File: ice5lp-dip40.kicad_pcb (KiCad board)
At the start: 2 copper layers, 17.8 x 50.8 mm, 6 parts, among them J1 Conn_02x04_Odd_Even, J2 Conn_01x20, J3 Conn_01x20, U1 AT25D011-SSHF, U2 MIC5355-S4YMME, U3 ICE5LP4K-SG48

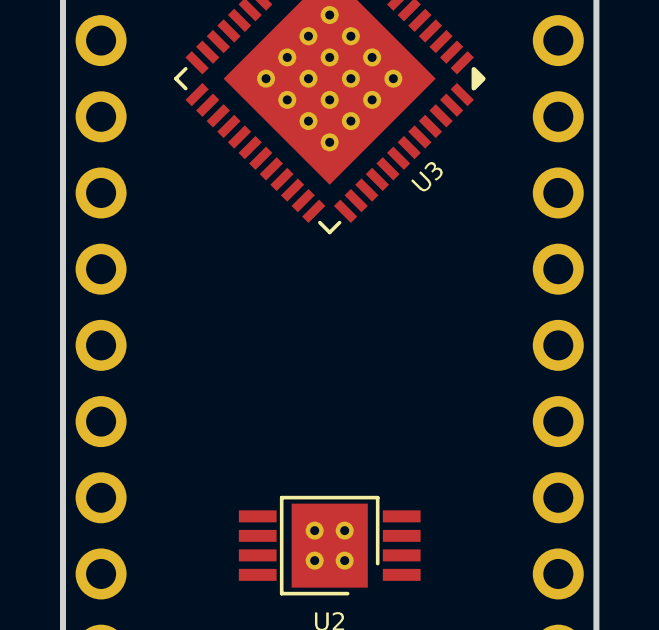
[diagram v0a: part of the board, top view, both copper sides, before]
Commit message: Add RGB LED and assign some FPGA IO to pin headers
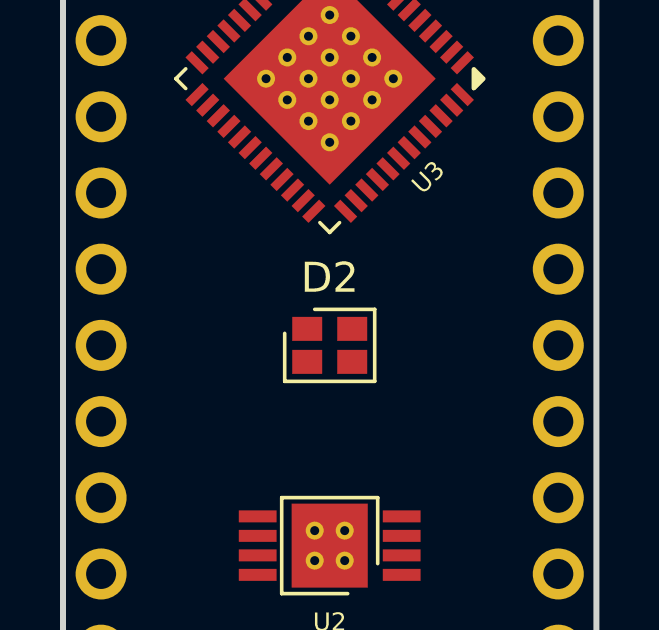
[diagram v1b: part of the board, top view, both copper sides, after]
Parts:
- added D2: CLMVC-FKC-CGJJM569aBB7a343, esynr3z_LED:LED_Cree-PLCC4_2x2mm_CW, F.Cu at (195.6, 91.4)
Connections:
- net Net-(J2-Pad10) renamed IOB_38B
- net Net-(J2-Pad11) renamed IOB_41A
- net Net-(J2-Pad12) renamed IOB_42B
- net Net-(J2-Pad13) renamed IOB_43A
- net Net-(J2-Pad14) renamed IOB_44B
- net Net-(J2-Pad15) renamed IOB_46B
- net Net-(J2-Pad16) renamed IOB_48B
- net Net-(J2-Pad17) renamed IOB_45A
- net Net-(J2-Pad18) renamed IOB_50B
- net Net-(J2-Pad7) renamed IOB_37A
- net Net-(J2-Pad8) renamed IOB_36B
- net Net-(J2-Pad9) renamed IOB_39A
- J2 pad 1: Net-(J2-Pad1) -> GND
- J2 pad 19: Net-(J2-Pad19) -> +5V
- J2 pad 2: Net-(J2-Pad2) -> IOB_24A
- J2 pad 20: Net-(J2-Pad20) -> GND
- J2 pad 3: Net-(J2-Pad3) -> IOB_31B
- J2 pad 4: Net-(J2-Pad4) -> IOB_29B
- J2 pad 5: Net-(J2-Pad5) -> IOB_25B
- J2 pad 6: Net-(J2-Pad6) -> IOB_23B
- J3 pad 1: Net-(J3-Pad1) -> GND
- J3 pad 19: Net-(J3-Pad19) -> +5V
- J3 pad 20: Net-(J3-Pad20) -> GND

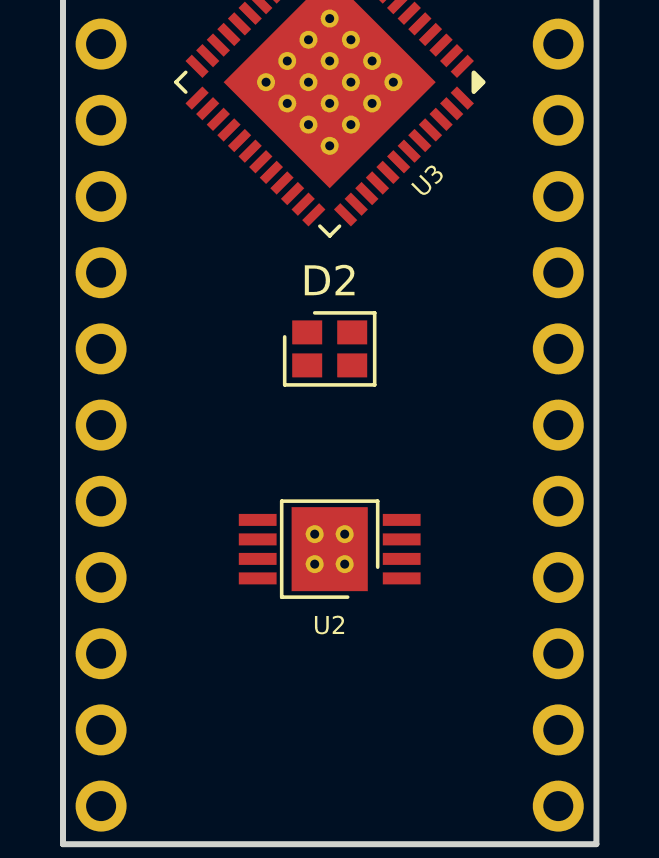
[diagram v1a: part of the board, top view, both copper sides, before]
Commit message: Add oscillator
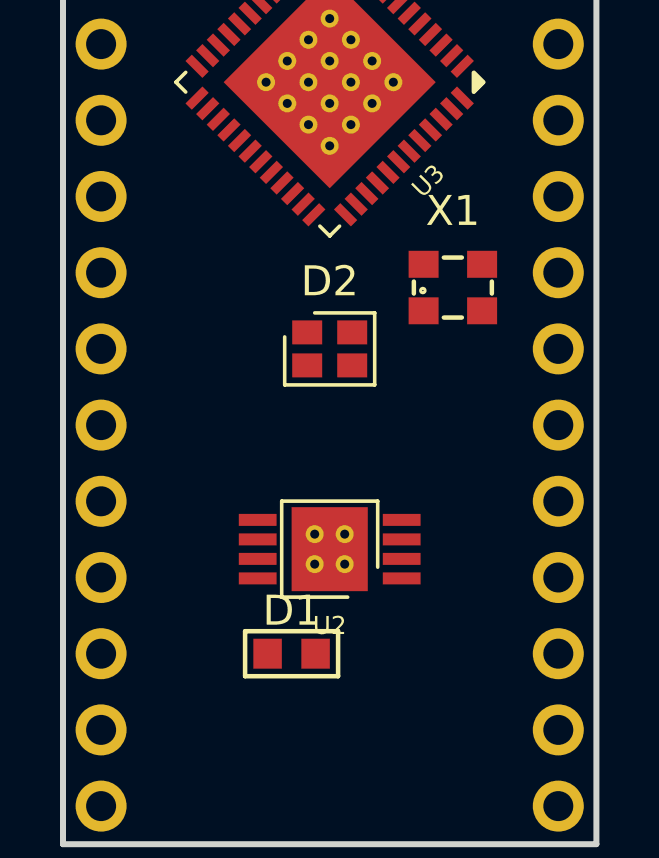
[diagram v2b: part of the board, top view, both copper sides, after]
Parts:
- added D1: CDBU0520, esynr3z_Diode:SOD-523F, F.Cu at (194.3, 101.6)
- added X1: ECS-2520MV-500-BN-TR, esynr3z_Oscillator:ECS-2520MV_4Pin_2.5x2.0mm, F.Cu at (199.7, 89.4)
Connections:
- J2 pad 10: IOB_38B -> IOT_38B
- J2 pad 11: IOB_41A -> IOT_41A
- J2 pad 13: IOB_43A -> IOT_43A
- J2 pad 14: IOB_44B -> IOT_44B
- J2 pad 15: IOB_46B -> IOT_46B
- J2 pad 16: IOB_48B -> IOT_48B
- J2 pad 17: IOB_45A -> IOT_45A
- J2 pad 18: IOB_50B -> IOT_50B
- J2 pad 5: IOB_25B -> Net-(J2-Pad5)
- J2 pad 7: IOB_37A -> IOT_37A
- J2 pad 8: IOB_36B -> IOT_36B
- J2 pad 9: IOB_39A -> IOT_39A
- U3 pad 20: IOB_25B -> ICE_CLK

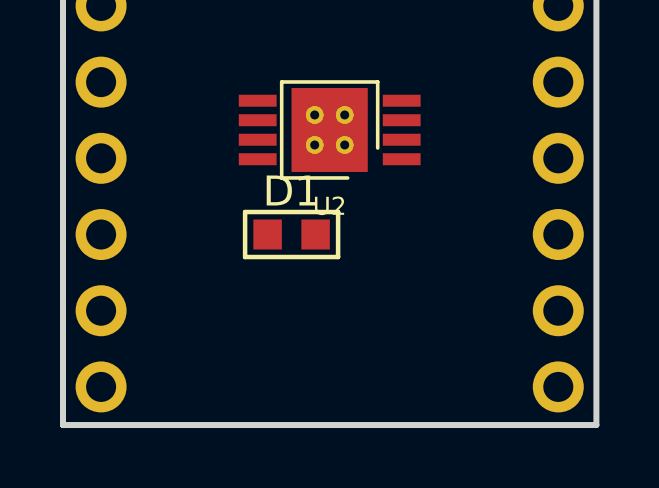
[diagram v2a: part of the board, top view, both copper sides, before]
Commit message: Add USB connector
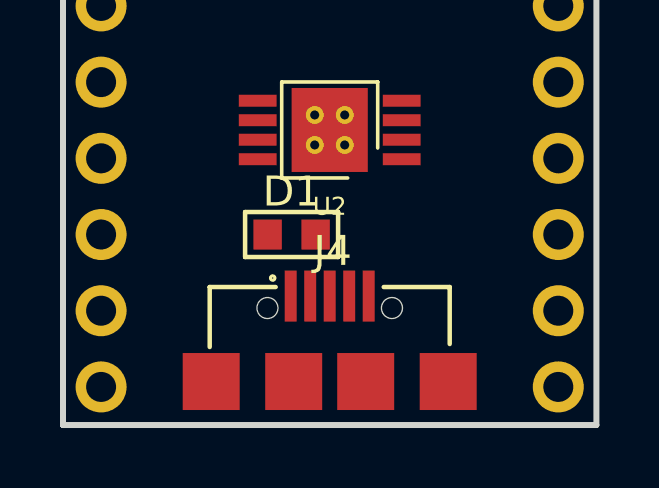
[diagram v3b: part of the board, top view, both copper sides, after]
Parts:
- added J4: USB_B_Micro, esynr3z_ConnectorUSB:USB_Micro-B_Wurth_629105136821, F.Cu at (195.6, 108.0)
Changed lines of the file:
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@@
     (tracks 0)
     (zones 0)
-    (modules 9)
-    (nets 74)
+    (modules 10)
+    (nets 77)
   )
   (page A4)
@@
     (31 B.Cu signal)
     (36 B.SilkS user hide)
-    (37 F.SilkS user hide)
+    (37 F.SilkS user)
     (38 B.Mask user)
     (39 F.Mask user)
@@
   (net 72 "Net-(D1-Pad1)")
   (net 73 ICE_CLK)
+  (net 74 "Net-(J4-Pad2)")
+  (net 75 "Net-(J4-Pad3)")
+  (net 76 "Net-(J4-Pad4)")
   (net_class Default "This is the default net class."
     (clearance 0.2)
@@
     (add_net "Net-(J3-Pad8)")
     (add_net "Net-(J3-Pad9)")
+    (add_net "Net-(J4-Pad2)")
+    (add_net "Net-(J4-Pad3)")
+    (add_net "Net-(J4-Pad4)")
     (add_net "Net-(R2-Pad2)")
     (add_net "Net-(R4-Pad2)")
@@
       (at (xyz 0 0 0))
       (scale (xyz 1 1 1))
+      (rotate (xyz 0 0 0))
+    )
+  )
+  (module esynr3z_ConnectorUSB:USB_Micro-B_Wurth_629105136821 (layer F.Cu)
+    (at 195.58 107.95)
+    (descr "USB Micro-B receptacle")
+    (tags "usb micro receptacle")
+    (attr smd)
+    (fp_text reference J4 (at 0.1 -5.8) (layer F.SilkS)
+      (effects (font (size 1 1) (thickness 0.15)))
+    )
+    (fp_text value USB_B_Micro (at 0 5.6) (layer F.Fab)
+      (effects (font (size 1 1) (thickness 0.15)))
+    )
+    (fp_line (start -4 -4.6) (end -4 1.3) (layer F.Fab) (width 0.15))
+    (fp_line (start -4 -0.65) (end -3.7 -0.65) (layer F.Fab) (width 0.15))
+    (fp_line (start -4 1.3) (end 4 1.3) (layer F.Fab) (width 0.15))
+    (fp_line (start 3.7 -0.65) (end 4 -0.65) (layer F.Fab) (width 0.15))
+    (fp_line (start 4 1.3) (end 4 -4.6) (layer F.Fab) (width 0.15))
+    (fp_line (start 4 -4.6) (end -4 -4.6) (layer F.Fab) (width 0.15))
+    (fp_line (start -2.7 0) (end 2.7 0) (layer F.Fab) (width 0.15))
+    (fp_line (start -1.075 -4.825) (end -1.3 -4.65) (layer F.Fab) (width 0.15))
+    (fp_line (start -1.3 -4.65) (end -1.525 -4.825) (layer F.Fab) (width 0.15))
+    (fp_line (start -1.525 -4.825) (end -1.525 -5.05) (layer F.Fab) (width 0.15))
+    (fp_line (start -1.525 -5.05) (end -1.075 -5.05) (layer F.Fab) (width 0.15))
+    (fp_line (start -1.075 -5.05) (end -1.075 -4.825) (layer F.Fab) (width 0.15))
+    (fp_line (start -4 -4.6) (end -4 -2.6) (layer F.SilkS) (width 0.15))
+    (fp_line (start 4 -2.7) (end 4 -4.6) (layer F.SilkS) (width 0.15))
+    (fp_line (start -1.8 -4.6) (end -4 -4.6) (layer F.SilkS) (width 0.15))
+    (fp_line (start 1.8 -4.6) (end 4 -4.6) (layer F.SilkS) (width 0.15))
+    (fp_line (start -5 -5.1) (end -5 1.4) (layer F.CrtYd) (width 0.05))
+    (fp_line (start -5 1.4) (end 5 1.4) (layer F.CrtYd) (width 0.05))
+    (fp_line (start 5 1.4) (end 5 -5.1) (layer F.CrtYd) (width 0.05))
+    (fp_line (start 5 -5.1) (end -5 -5.1) (layer F.CrtYd) (width 0.05))
+    (fp_text user %R (at 0 -2.75) (layer F.Fab)
+      (effects (font (size 1 1) (thickness 0.15)))
+    )
+    (fp_text user "PCB Edge" (at 0 -0.05) (layer Dwgs.User)
+      (effects (font (size 0.5 0.5) (thickness 0.08)))
+    )
+    (fp_circle (center -1.9 -4.9) (end -1.85 -4.9) (layer F.SilkS) (width 0.15))
+    (pad 1 smd rect (at -1.3 -4.3) (size 0.4 1.7) (layers F.Cu F.Paste F.Mask)
+      (net 32 +5V))
+    (pad 2 smd rect (at -0.65 -4.3) (size 0.4 1.7) (layers F.Cu F.Paste F.Mask)
+      (net 74 "Net-(J4-Pad2)"))
+    (pad 3 smd rect (at 0 -4.3) (size 0.4 1.7) (layers F.Cu F.Paste F.Mask)
+      (net 75 "Net-(J4-Pad3)"))
+    (pad 4 smd rect (at 0.65 -4.3) (size 0.4 1.7) (layers F.Cu F.Paste F.Mask)
+      (net 76 "Net-(J4-Pad4)"))
+    (pad 5 smd rect (at 1.3 -4.3) (size 0.4 1.7) (layers F.Cu F.Paste F.Mask)
+      (net 2 GND))
+    (pad "" np_thru_hole oval (at -2.075 -3.9) (size 0.7 0.7) (drill 0.7) (layers *.Cu *.Mask))
+    (pad "" np_thru_hole oval (at 2.075 -3.9) (size 0.7 0.7) (drill 0.7) (layers *.Cu *.Mask))
+    (pad 6 smd rect (at 1.2 -1.45) (size 1.9 1.9) (layers F.Cu F.Paste F.Mask)
+      (net 2 GND))
+    (pad 6 smd rect (at 3.95 -1.45) (size 1.9 1.9) (layers F.Cu F.Paste F.Mask)
+      (net 2 GND))
+    (pad 6 smd rect (at -1.2 -1.45) (size 1.9 1.9) (layers F.Cu F.Paste F.Mask)
+      (net 2 GND))
+    (pad 6 smd rect (at -3.95 -1.45) (size 1.9 1.9) (layers F.Cu F.Paste F.Mask)
+      (net 2 GND))
+    (model ${KISYS3DMOD}/Connector_USB.3dshapes/USB_Micro-B_Wuerth_629105150521.wrl
+      (at (xyz 0 0 0))
+      (scale (xyz 1 1 1))

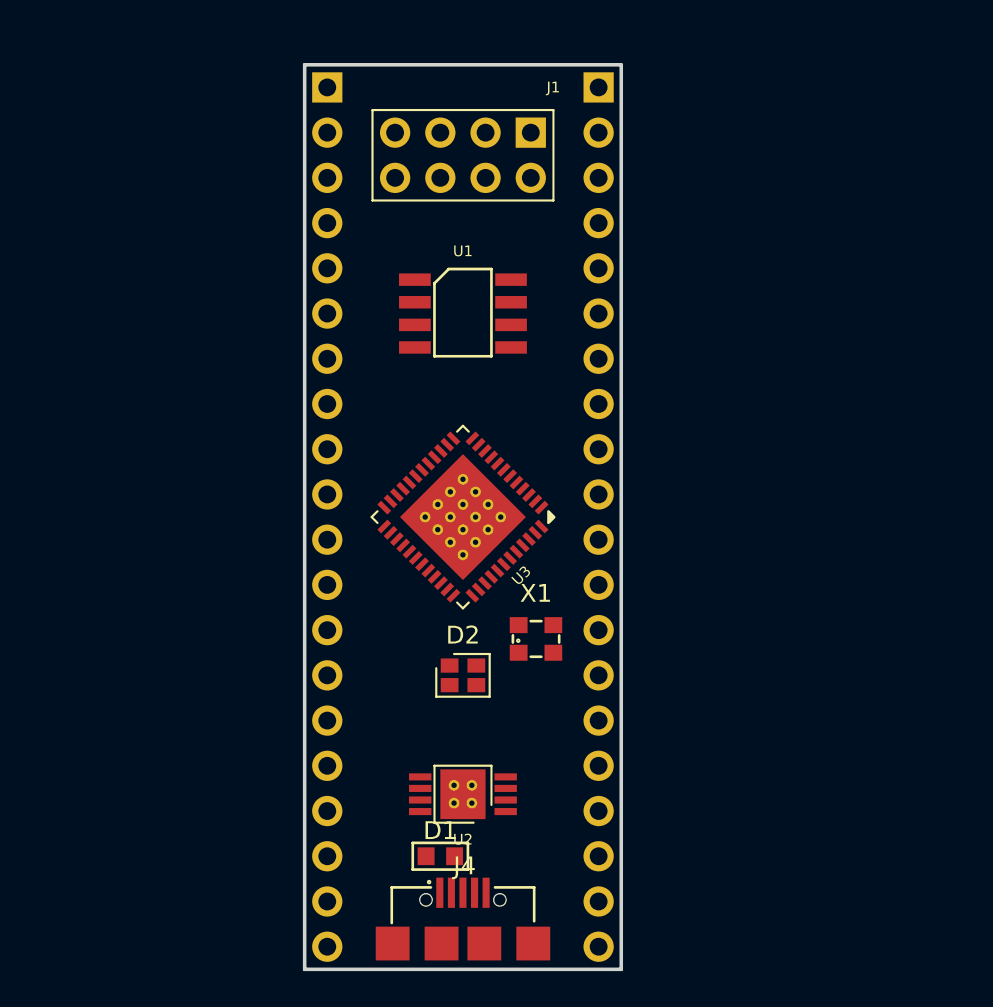
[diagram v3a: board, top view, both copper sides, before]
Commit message: Add footprints to some symbols and trace pin headers and buttons
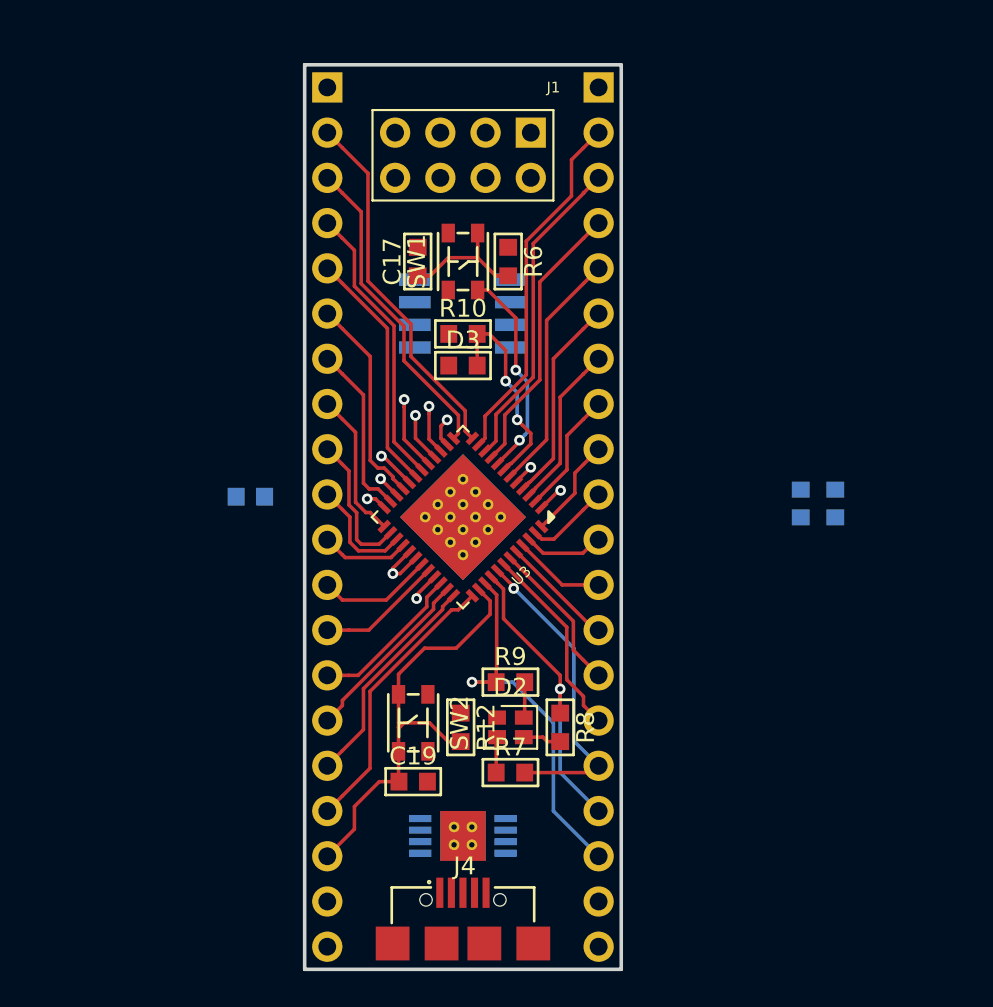
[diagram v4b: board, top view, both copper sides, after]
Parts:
- added C17: 100n, esynr3z_Passive:0603, F.Cu at (193.0, 68.2)
- added C19: 100n, esynr3z_Passive:0603, F.Cu at (192.8, 97.4)
- added D3: LED_GREEN, esynr3z_Passive:0603, F.Cu at (195.6, 74.0)
- added R10: 1k, esynr3z_Passive:0603, F.Cu at (195.6, 72.3)
- added R12: 10k, esynr3z_Passive:0603, F.Cu at (195.5, 94.4)
- added R6: 10k, esynr3z_Passive:0603, F.Cu at (198.1, 68.2)
- added R7: 82, esynr3z_Passive:0603, F.Cu at (198.2, 96.9)
- added R8: 22, esynr3z_Passive:0603, F.Cu at (201.0, 94.4)
- added R9: 22, esynr3z_Passive:0603, F.Cu at (198.2, 91.8)
- added SW1: SW_Push, esynr3z_Switch:PTS830, F.Cu at (195.6, 68.2)
- added SW2: SW_Push, esynr3z_Switch:PTS830, F.Cu at (192.8, 94.1)
- D1, U1, U2, X1: moved to B.Cu
- moved D1 22.8 mm to (183.6, 81.4)
- moved X1 17.6 mm to (215.5, 81.8)
- moved D2 3.96 mm to (198.2, 94.4)
- moved U2 2.34 mm to (195.6, 100.5), turned to 0 degrees
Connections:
- net IOT_50B renamed ICE_BTN
- J2 pad 12: IOB_42B -> IOT_42B
- J2 pad 2: IOB_24A -> IOB_22A
- J2 pad 3: IOB_31B -> IOB_24A
- J2 pad 4: IOB_29B -> IOB_31B
- J2 pad 5: Net-(J2-Pad5) -> IOB_29B
- J3 pad 10: Net-(J3-Pad10) -> IOB_2A
- J3 pad 11: Net-(J3-Pad11) -> IOB_0A
- J3 pad 12: Net-(J3-Pad12) -> IOB_5B
- J3 pad 13: Net-(J3-Pad13) -> IOB_3B
- J3 pad 14: Net-(J3-Pad14) -> IOT_49A
- J3 pad 15: Net-(J3-Pad15) -> IOT_51A
- J3 pad 16: Net-(J3-Pad16) -> RGB_R
- J3 pad 17: Net-(J3-Pad17) -> RGB_G
- J3 pad 18: Net-(J3-Pad18) -> RGB_B
- J3 pad 2: Net-(J3-Pad2) -> IOB_20A
- J3 pad 3: Net-(J3-Pad3) -> IOB_18A
- J3 pad 4: Net-(J3-Pad4) -> IOB_16A
- J3 pad 5: Net-(J3-Pad5) -> IOB_13B
- J3 pad 6: Net-(J3-Pad6) -> IOB_8A
- J3 pad 7: Net-(J3-Pad7) -> IOB_9B
- J3 pad 8: Net-(J3-Pad8) -> IOB_6A
- J3 pad 9: Net-(J3-Pad9) -> IOB_4A
- U3 pad 29: VCC_PLL -> VCC_CORE
- U3 pad 39: RGB2 -> RGB_B
- U3 pad 40: RGB1 -> RGB_G
- U3 pad 41: RGB0 -> RGB_R
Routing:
- net ICE_BTN: track 0.00 -> 24.8 mm
- net RGB_B: track 0.00 -> 21.3 mm, vias 0 -> 1
- net IOB_22A: track 0.00 -> 20.5 mm
- net IOB_20A: track 0.00 -> 20.3 mm
- net CRESET: track 0.00 -> 19.2 mm, vias 0 -> 2
- net IOB_18A: track 0.00 -> 18.2 mm
- net IOB_24A: track 0.00 -> 17.8 mm
- net RGB_R: track 0.00 -> 17.6 mm, vias 0 -> 1
- net RGB_G: track 0.00 -> 17.0 mm, vias 0 -> 1
- net IOB_31B: track 0.00 -> 16.1 mm
- net IOT_45A: track 0.00 -> 15.7 mm
- net IOB_16A: track 0.00 -> 15.6 mm
- net IOB_13B: track 0.00 -> 13.7 mm
- net IOB_29B: track 0.00 -> 13.7 mm
- net IOT_48B: track 0.00 -> 12.5 mm
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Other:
- net class Default: clearance 0.2 -> 0.17; via_dia 0.8 -> 0.6; via_drill 0.4 -> 0.3
- rule trace_clearance: 0.2 -> 0.17

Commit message: Update footprints
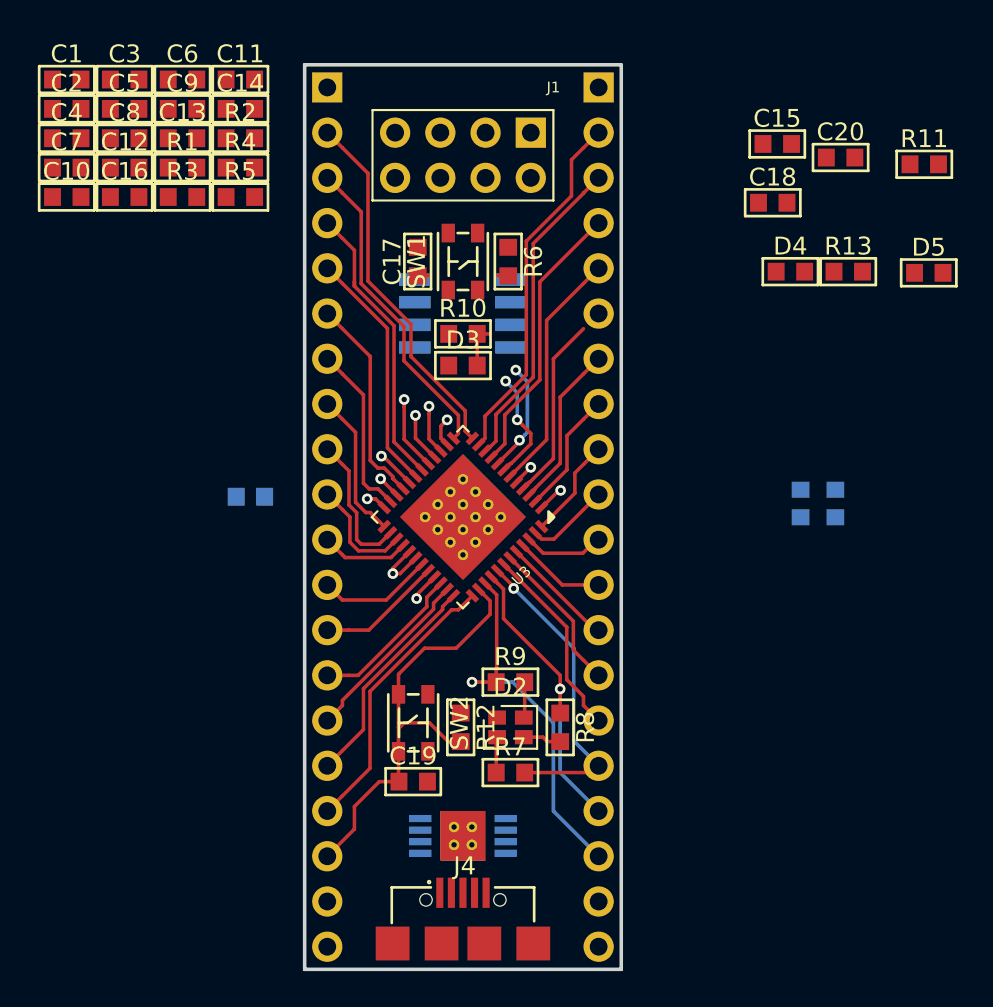
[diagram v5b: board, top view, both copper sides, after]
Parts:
- added C1: 1u, esynr3z_Capacitor:C_0603, F.Cu at (173.3, 58.0)
- added C10: 100n, esynr3z_Capacitor:C_0603, F.Cu at (173.3, 64.6)
- added C11: 100n, esynr3z_Capacitor:C_0603, F.Cu at (183.1, 58.0)
- added C12: 1u, esynr3z_Capacitor:C_0603, F.Cu at (176.6, 62.9)
- added C13: 100n, esynr3z_Capacitor:C_0603, F.Cu at (179.8, 61.3)
- added C14: 1u, esynr3z_Capacitor:C_0603, F.Cu at (183.1, 59.6)
- added C15: 100n, esynr3z_Capacitor:C_0603, F.Cu at (213.2, 61.6)
- added C16: 100n, esynr3z_Capacitor:C_0603, F.Cu at (176.6, 64.6)
- added C18: 100n, esynr3z_Capacitor:C_0603, F.Cu at (213.0, 64.9)
- added C2: 100n, esynr3z_Capacitor:C_0603, F.Cu at (173.3, 59.6)
- added C20: 10u, esynr3z_Capacitor:C_0603, F.Cu at (216.8, 62.4)
- added C3: 2.2u, esynr3z_Capacitor:C_0603, F.Cu at (176.6, 58.0)
- added C4: 100n, esynr3z_Capacitor:C_0603, F.Cu at (173.3, 61.3)
- added C5: 1u, esynr3z_Capacitor:C_0603, F.Cu at (176.6, 59.6)
- added C6: 100n, esynr3z_Capacitor:C_0603, F.Cu at (179.8, 58.0)
- added C7: 2.2u, esynr3z_Capacitor:C_0603, F.Cu at (173.3, 62.9)
- added C8: 2.2u, esynr3z_Capacitor:C_0603, F.Cu at (176.6, 61.3)
- added C9: 1u, esynr3z_Capacitor:C_0603, F.Cu at (179.8, 59.6)
- added D4: LED_RED, esynr3z_LED:LED_0603, F.Cu at (214.0, 68.8)
- added D5: LED_ORANGE, esynr3z_LED:LED_0603, F.Cu at (221.7, 68.8)
- added R1: 10k, esynr3z_Resistor:R_0603, F.Cu at (179.8, 62.9)
- added R11: 2.2k, esynr3z_Resistor:R_0603, F.Cu at (221.5, 62.7)
- added R13: 1k, esynr3z_Resistor:R_0603, F.Cu at (217.2, 68.8)
- added R2: 10k, esynr3z_Resistor:R_0603, F.Cu at (183.1, 61.3)
- added R3: 100, esynr3z_Resistor:R_0603, F.Cu at (179.8, 64.6)
- added R4: 10k, esynr3z_Resistor:R_0603, F.Cu at (183.1, 62.9)
- added R5: 10k, esynr3z_Resistor:R_0603, F.Cu at (183.1, 64.6)
- C17, C19: footprint esynr3z_Passive:0603 -> esynr3z_Capacitor:C_0603
- D3: footprint esynr3z_Passive:0603 -> esynr3z_LED:LED_0603
- R10, R12, R6, R7, R8, R9: footprint esynr3z_Passive:0603 -> esynr3z_Resistor:R_0603
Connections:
- J4 pad 2: Net-(J4-Pad2) -> (no net)
- J4 pad 3: Net-(J4-Pad3) -> (no net)
- J4 pad 4: Net-(J4-Pad4) -> (no net)
- U2 pad 3: Net-(U2-Pad3) -> (no net)
- U2 pad 6: Net-(U2-Pad6) -> (no net)
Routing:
- net CRESET: track 19.2 -> 7.61 mm
- net CDONE: track 11.7 -> 8.68 mm
- net IOB_8A: track 11.6 -> 10.4 mm
